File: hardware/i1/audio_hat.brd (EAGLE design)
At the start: 66.8 x 56.5 mm, 6 parts

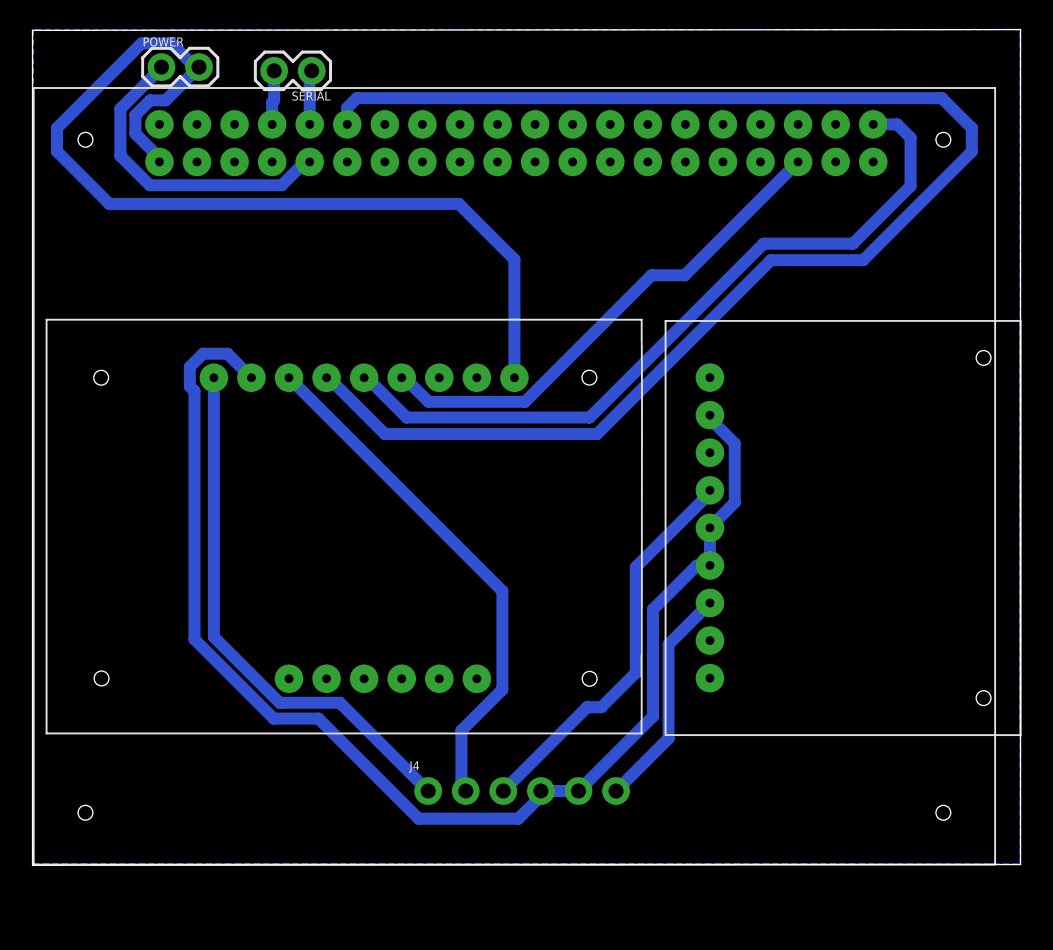
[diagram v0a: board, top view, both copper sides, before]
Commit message: Correct via routing on top layer
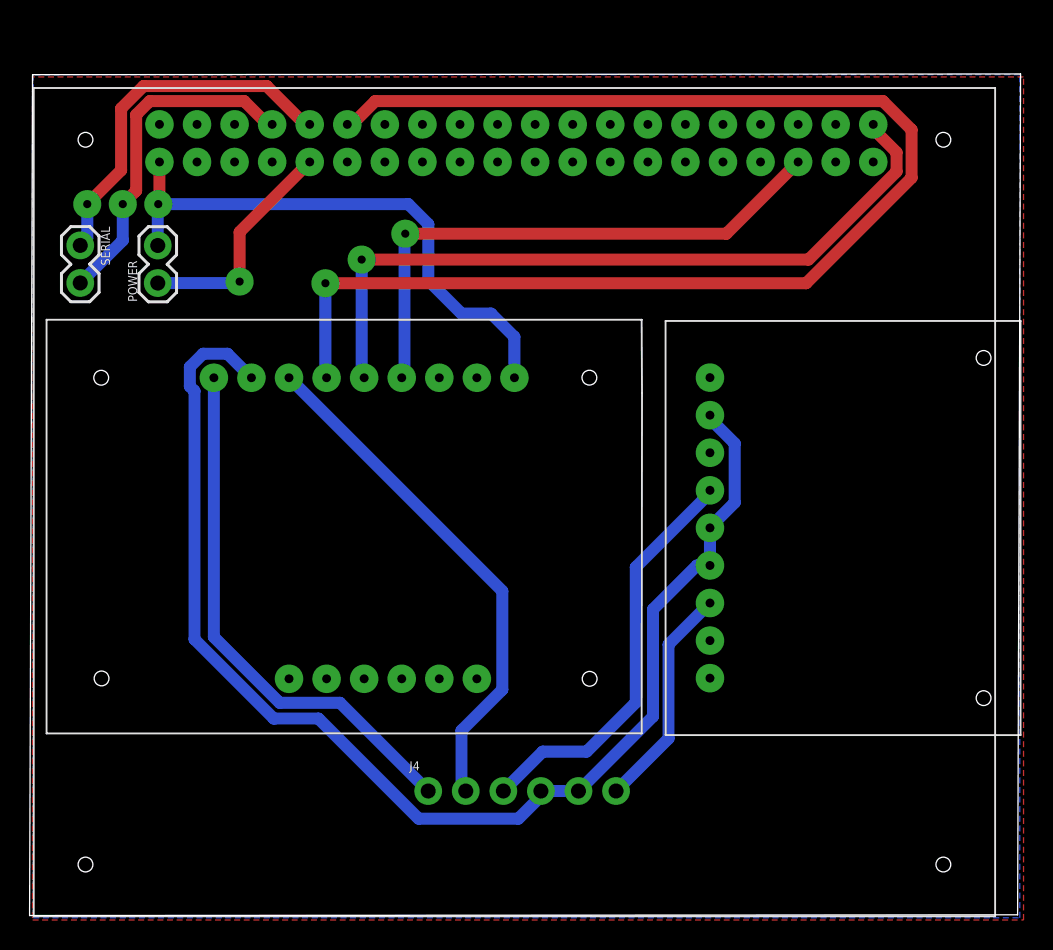
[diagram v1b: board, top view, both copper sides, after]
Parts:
- moved SERIAL 19.6 mm to (11.2, 80.6), turned to 270 degrees
- moved POWER 14.6 mm to (16.5, 78.1), turned to 90 degrees
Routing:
- net N$3: track 65.5 -> 38.5 mm, vias 0 -> 1
- net N$11: track 3.68 -> 24.9 mm, vias 0 -> 1
- net N$9: track 3.68 -> 23.2 mm, vias 0 -> 1
- net N$12: track 99.2 -> 91.9 mm, vias 0 -> 1
- net N$2: track 21.4 -> 15.6 mm, vias 0 -> 1
- net N$1: track 34.2 -> 38.4 mm, vias 0 -> 1
- net N$8: track 26.7 -> 27.9 mm
- net N$4: track 50.7 -> 50.5 mm, vias 0 -> 1
- added copper zone on layer 1, net GND
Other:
- board size 66.8 x 56.5 mm -> 67 x 56.9 mm

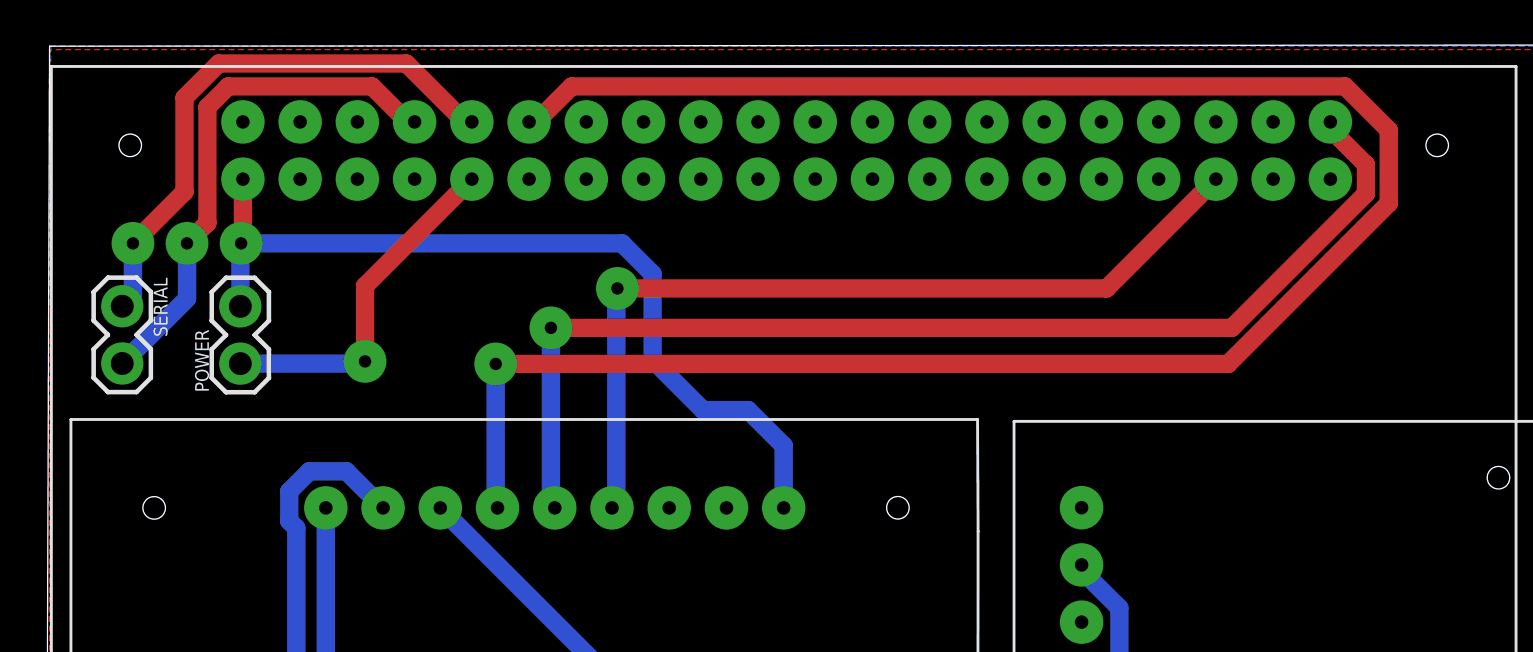
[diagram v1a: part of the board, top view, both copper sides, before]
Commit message: Audio hat now makes use of PCB via rivets
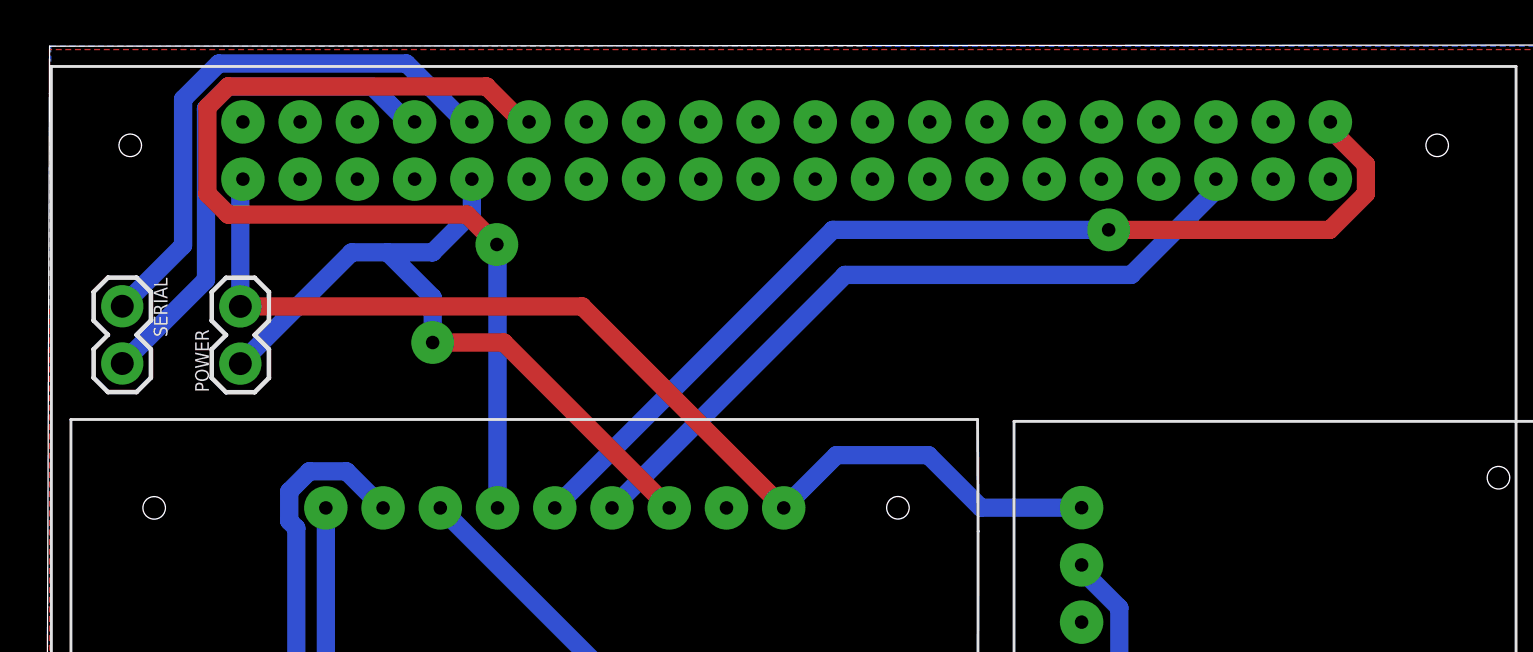
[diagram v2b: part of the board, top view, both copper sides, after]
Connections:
- removed net GND: RPI_3A+1.GND_C, UDA1.GND
- net N$2: now also UDA1.GND
- net N$3: now also MAX1.VDD
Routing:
- net N$12: track 91.9 -> 44.6 mm
- net N$2: track 15.6 -> 32.9 mm
- net N$3: track 38.5 -> 48.7 mm, vias 1 -> 0
- net N$1: track 38.4 -> 33.1 mm, vias 1 -> 0
- net N$4: track 50.5 -> 45.6 mm
- net N$9: vias 1 -> 0
- net N$11: vias 1 -> 0

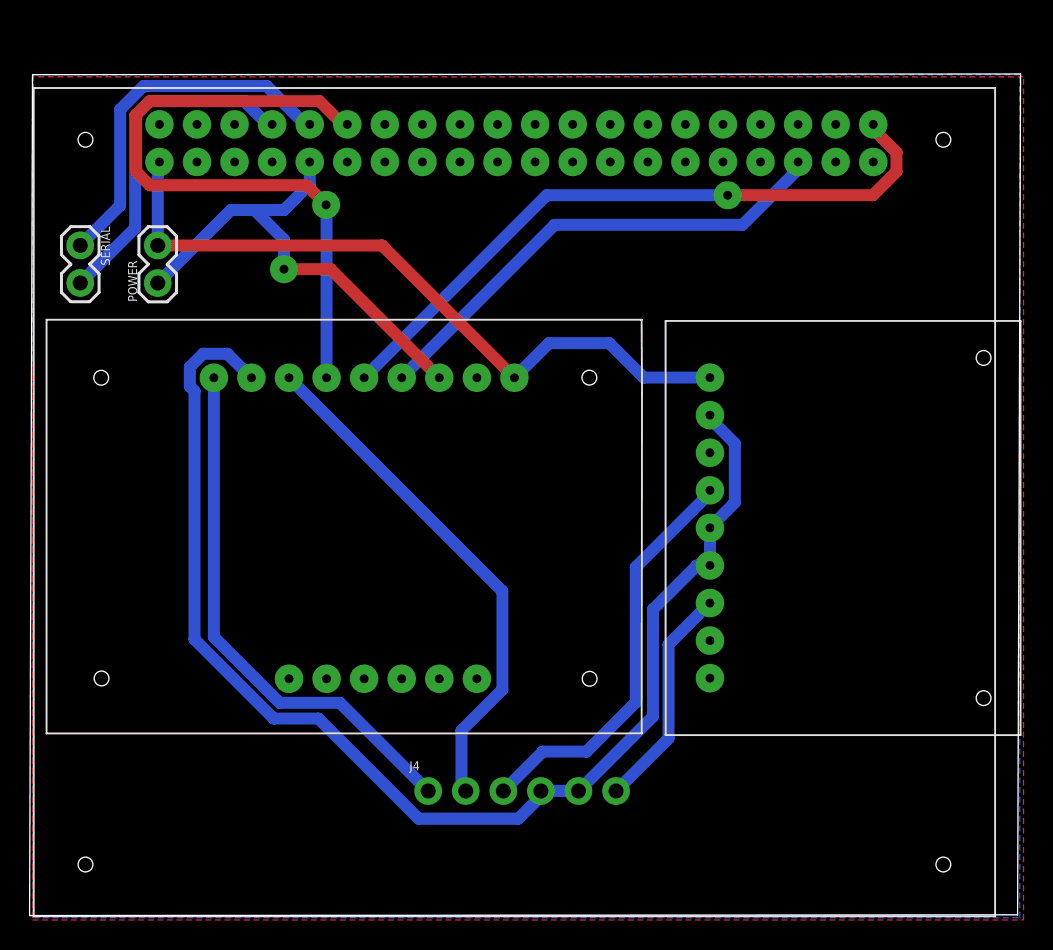
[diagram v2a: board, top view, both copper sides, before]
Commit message: Add wristband schematic and board layout
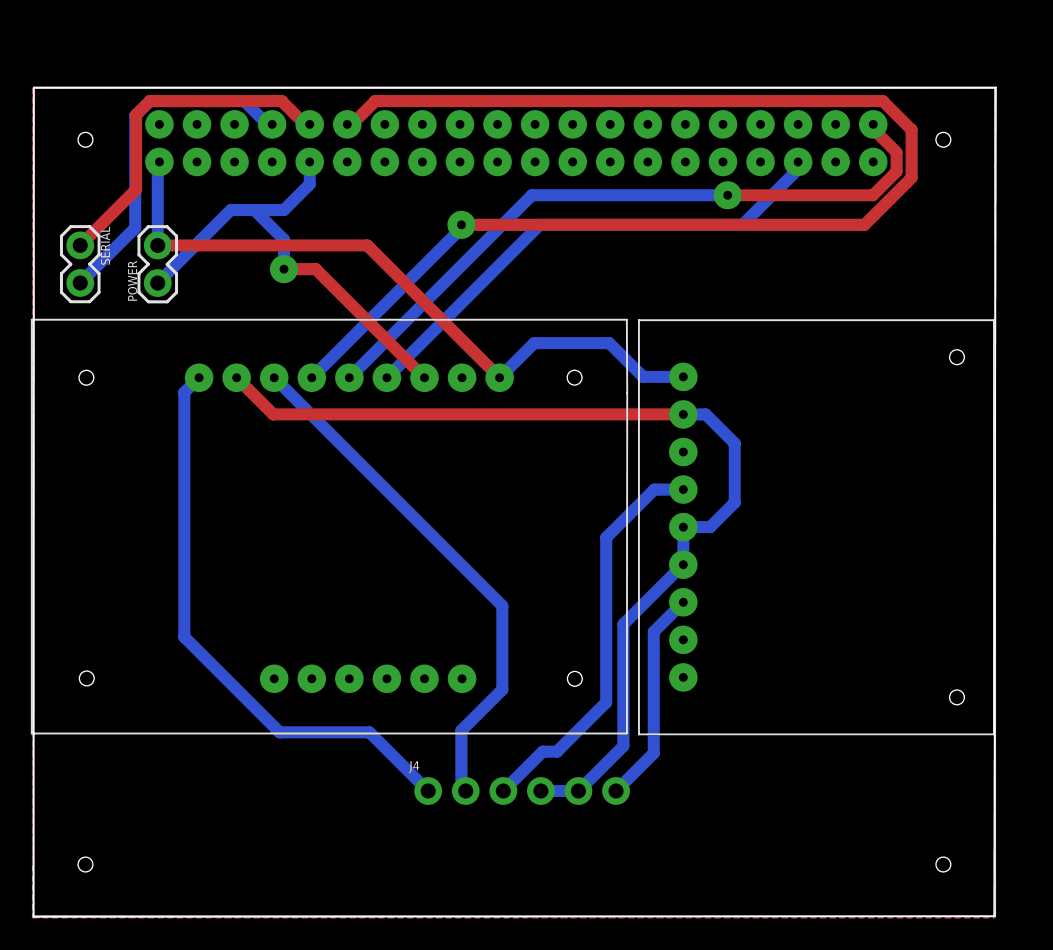
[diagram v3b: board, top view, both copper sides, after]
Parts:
- moved MAX1 1.80 mm to (52.0, 61.5)
- moved UDA1 1.00 mm to (48.1, 50.7)
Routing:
- net N$12: track 44.6 -> 89.1 mm
- net N$7: track 86.7 -> 67.0 mm
- net N$5: track 36.3 -> 38.7 mm
- net N$3: track 48.7 -> 46.8 mm
- net N$11: track 24.9 -> 23.2 mm
- net N$4: track 45.6 -> 46.6 mm
- net N$1: track 33.1 -> 34.1 mm
- net N$2: track 32.9 -> 31.9 mm
- net N$8: track 27.9 -> 27.1 mm
- net N$10: track 15.3 -> 14.6 mm
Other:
- board size 67 x 56.9 mm -> 65.1 x 56.1 mm

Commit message: Final tweaks for mechanical fit.
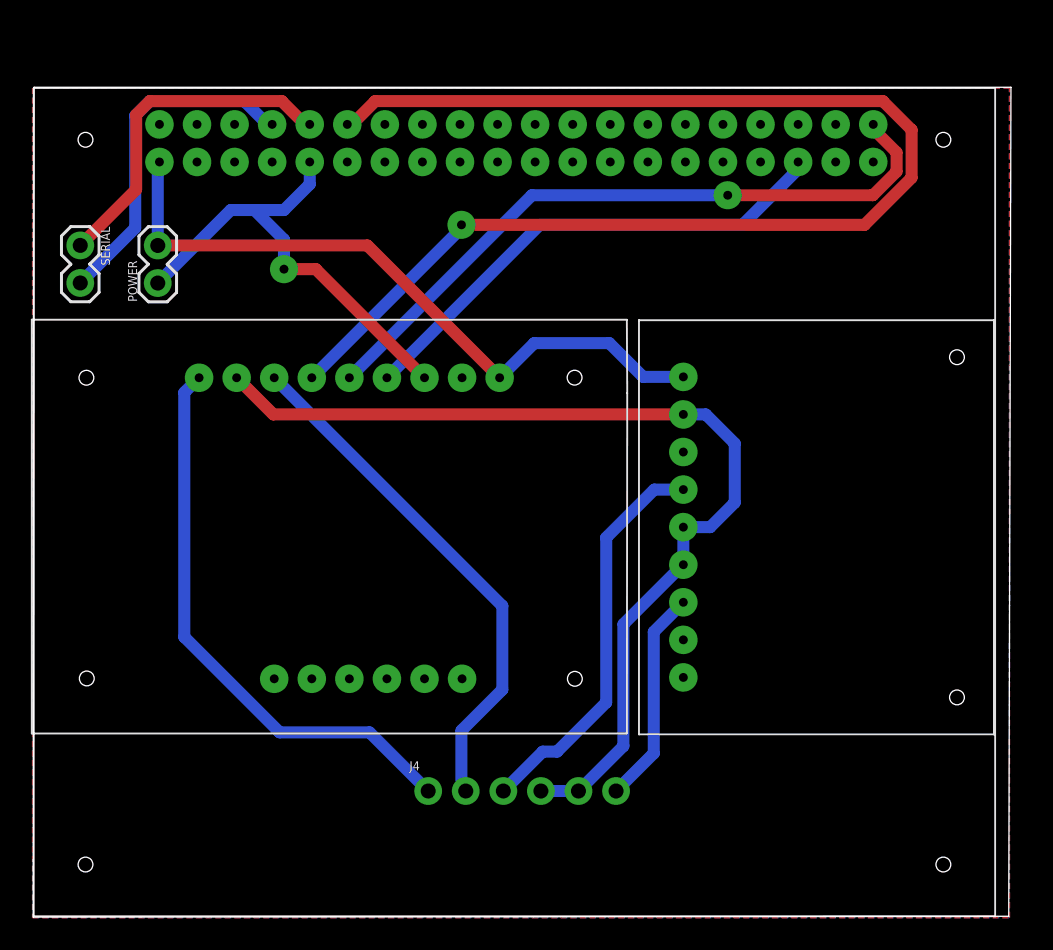
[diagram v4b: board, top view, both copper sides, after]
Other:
- board size 65.1 x 56.1 mm -> 66.1 x 56.1 mm
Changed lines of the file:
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@@
 <board>
 <plain>
-<wire x1="8.05" y1="35.2" x2="73" y2="35.25" width="0" layer="20"/>
-<wire x1="73" y1="35.25" x2="73.15" y2="91.3" width="0" layer="20"/>
-<wire x1="73.15" y1="91.3" x2="8.1" y2="91.3" width="0" layer="20"/>
+<wire x1="8.05" y1="35.2" x2="74" y2="35.25" width="0" layer="20"/>
+<wire x1="74" y1="35.25" x2="74.15" y2="91.3" width="0" layer="20"/>
+<wire x1="74.15" y1="91.3" x2="8.1" y2="91.3" width="0" layer="20"/>
 <wire x1="8.1" y1="91.3" x2="8.05" y2="35.2" width="0" layer="20"/>
 </plain>
@@
 <vertex x="8.05" y="91.25"/>
 <vertex x="8.05" y="35.15"/>
-<vertex x="73.05" y="35.15"/>
-<vertex x="73.05" y="91.25"/>
+<vertex x="74.05" y="35.15"/>
+<vertex x="74.05" y="91.25"/>
 </polygon>
 <polygon width="0.1524" layer="1">
 <vertex x="8" y="91.25"/>
 <vertex x="8" y="35.15"/>
-<vertex x="73.05" y="35.15"/>
-<vertex x="73.05" y="91.25"/>
+<vertex x="74.05" y="35.15"/>
+<vertex x="74.05" y="91.25"/>
 </polygon>
 </signal>
